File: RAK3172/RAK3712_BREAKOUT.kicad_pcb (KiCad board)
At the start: 2 copper layers, 26.9 x 52 mm, 5 parts, among them J1 Conn_01x20_Male, J2 Conn_01x20_Male, U1 RAK11300

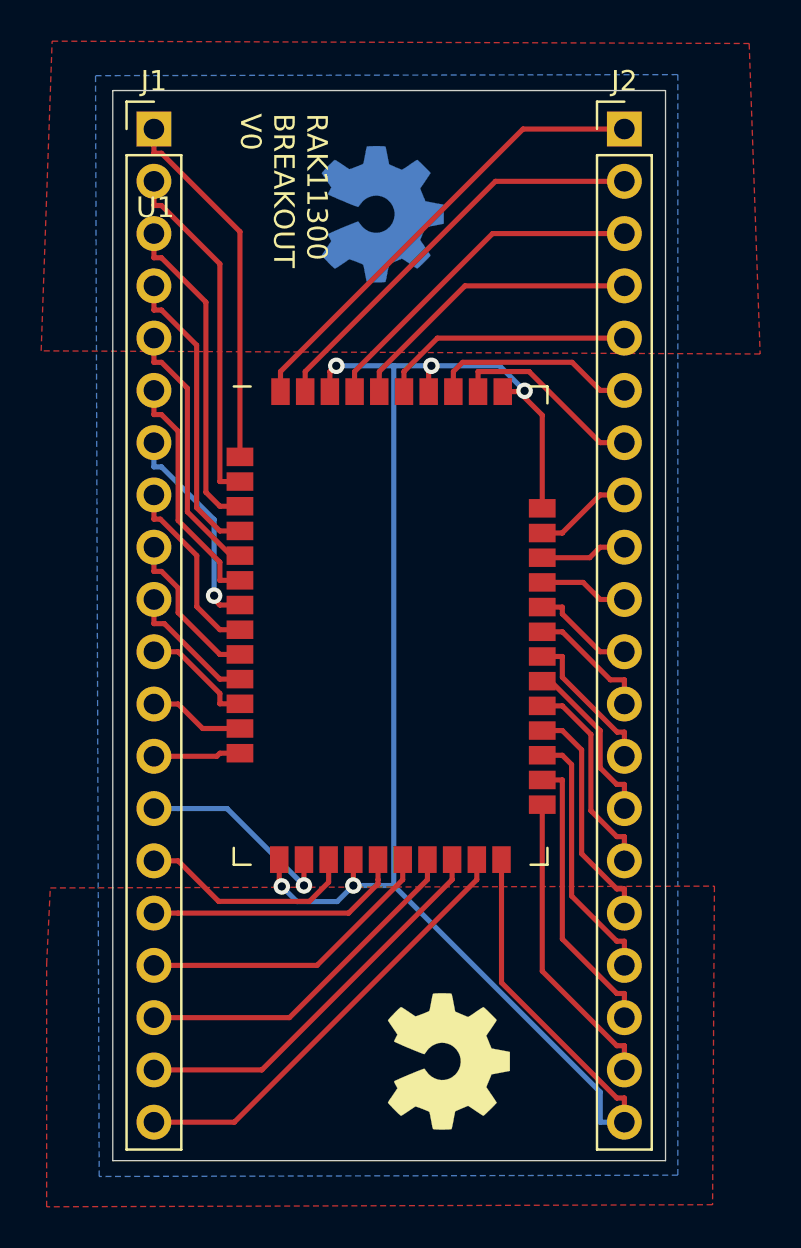
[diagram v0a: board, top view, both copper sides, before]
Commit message: foot:(DIL_BREAKOUT_PCB RAK 3712)ready for route
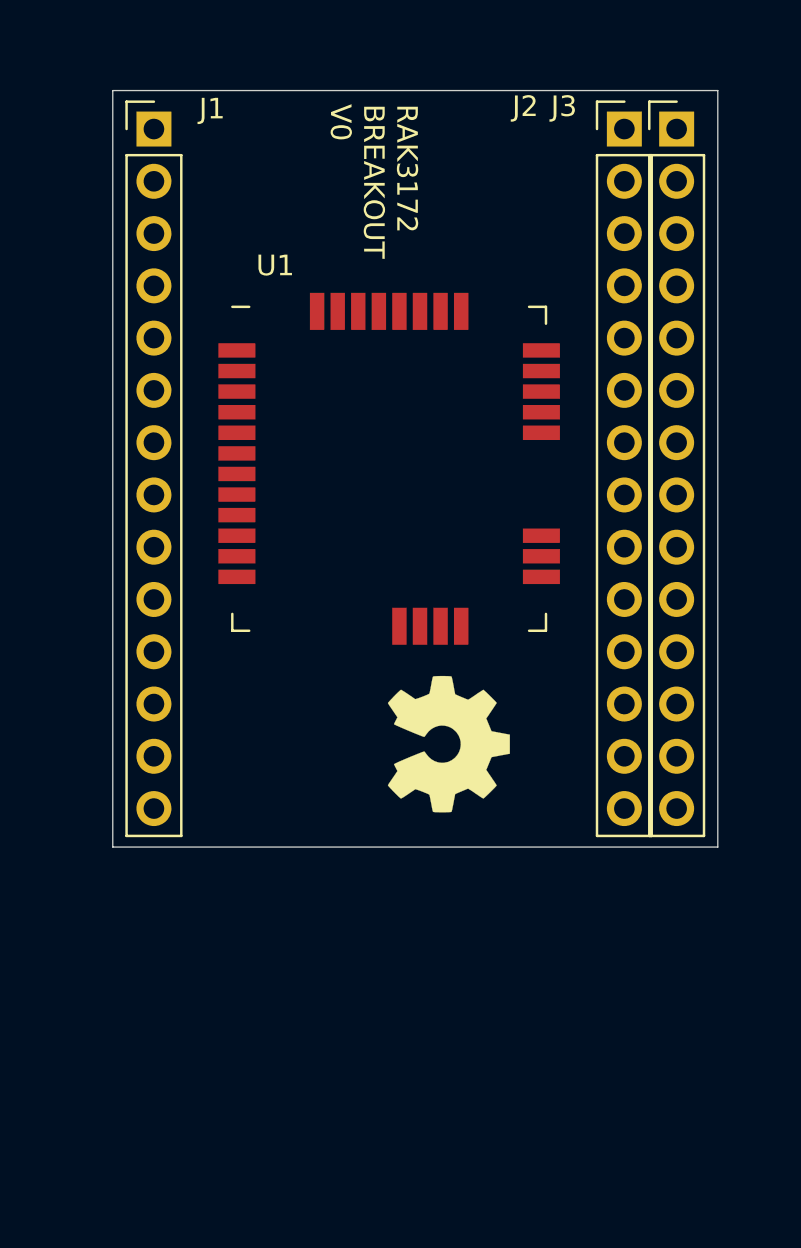
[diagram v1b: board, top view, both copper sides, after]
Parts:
- removed the REF** at (63.1, 56.0)
- added J3: Conn_01x14_Male, Connector_PinHeader_2.54mm:PinHeader_1x14_P2.54mm_Vertical, F.Cu at (77.4, 51.9)
- J1, J2: value Conn_01x20_Male -> Conn_01x14_Male; footprint Connector_PinHeader_2.54mm:PinHeader_1x20_P2.54mm_Vertical -> Connector_PinHeader_2.54mm:PinHeader_1x14_P2.54mm_Vertical
- U1: value RAK11300 -> RAK3712; footprint RAKWIRELESS:RAK11300 -> RAKWIRELESS:RAK3712
- moved REF** 15.4 mm to (66.3, 81.8)
- moved U1 7.62 mm to (63.4, 68.4)
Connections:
- J1 pad 14: /ICPIN15 -> /ICPIN14
- J2 pad 1: /ICPIN46 -> /ICPIN32
- J2 pad 10: /ICPIN33 -> /ICPIN21
- J2 pad 11: /ICPIN32 -> /ICPIN20
- J2 pad 12: /ICPIN31 -> /ICPIN19
- J2 pad 13: /ICPIN30 -> /ICPIN16
- J2 pad 14: /ICPIN29 -> /ICPIN15
- J2 pad 2: /ICPIN45 -> /ICPIN31
- J2 pad 3: /ICPIN43 -> /ICPIN30
- J2 pad 4: /ICPIN42 -> /ICPIN29
- J2 pad 5: /ICPIN41 -> /ICPIN27
- J2 pad 6: /ICPIN39 -> /ICPIN26
- J2 pad 7: /ICPIN38 -> /ICPIN25
- J2 pad 8: /ICPIN35 -> /ICPIN24
- J2 pad 9: /ICPIN34 -> /ICPIN22
- U1 pad 14: /ICPIN23 -> /ICPIN14
- U1 pad 17: /ICPIN23 -> /ICPIN11
- U1 pad 18: /ICPIN18 -> /ICPIN11
- U1 pad 23: /ICPIN23 -> /ICPIN11
- U1 pad 28: /ICPIN28 -> /ICPIN11
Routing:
- net /ICPIN23: track 85.7 -> 0.00 mm, vias 5 -> 0
- net /ICPIN46: track 22.6 -> 0.00 mm
- net /ICPIN22: track 21.5 -> 0.00 mm
- net /ICPIN45: track 20.3 -> 0.00 mm
- net /ICPIN21: track 19.3 -> 0.00 mm
- net /ICPIN01: track 17.9 -> 0.00 mm
- net /ICPIN02: track 17.1 -> 0.00 mm
- net /ICPIN20: track 17.0 -> 0.00 mm
- net /ICPIN43: track 16.9 -> 0.00 mm
- net /ICPIN03: track 15.8 -> 0.00 mm
- net /ICPIN19: track 14.8 -> 0.00 mm
- net /ICPIN24: track 14.8 -> 0.00 mm
- net /ICPIN42: track 14.6 -> 0.00 mm
- net /ICPIN04: track 14.4 -> 0.00 mm
- net /ICPIN25: track 14.0 -> 0.00 mm
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- removed copper zone on B.Cu, net /ICPIN23
- removed copper zone on F.Cu, net /ICPIN23
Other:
- board size 26.9 x 52 mm -> 29.4 x 36.8 mm
- board text added: "RAK3172 BREAKOUT V0"
- board text removed: "RAK11300 BREAKOUT V0"

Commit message: foot:(DIL_BREAKOUT_PCB RAK 3712)first route
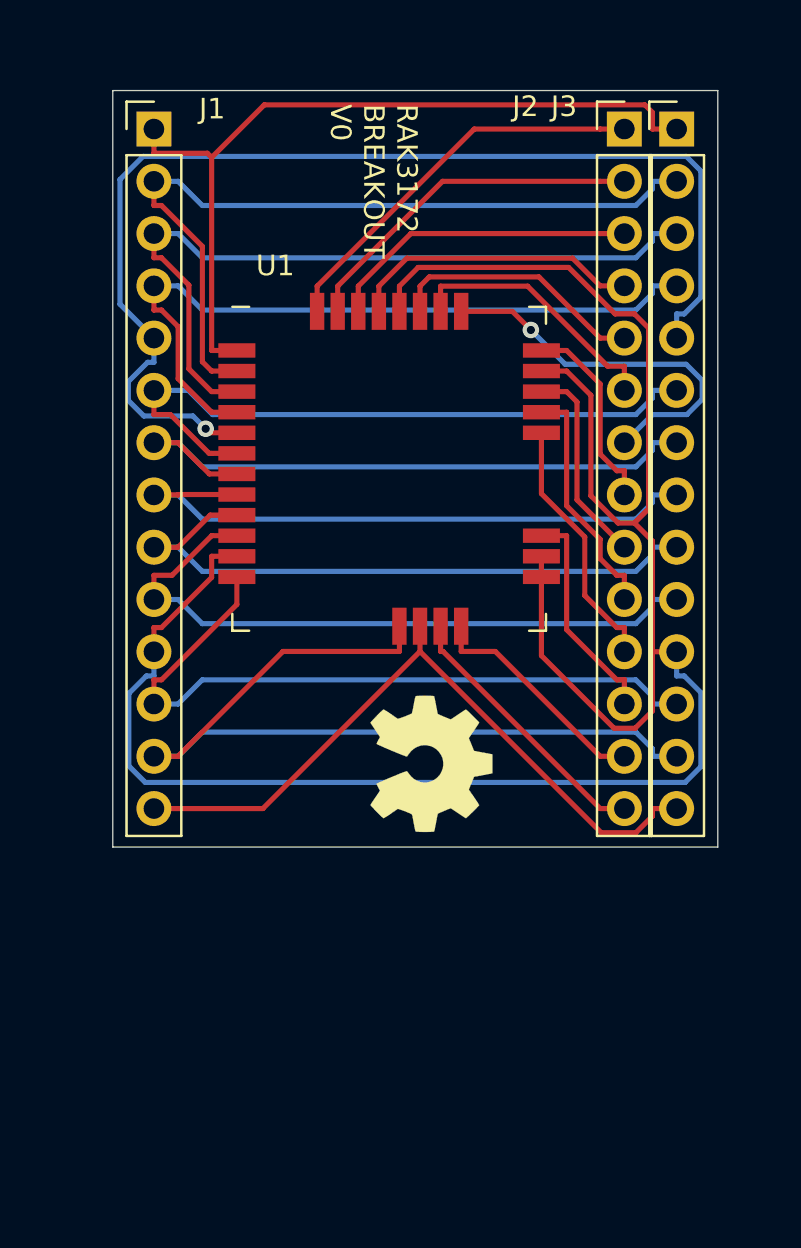
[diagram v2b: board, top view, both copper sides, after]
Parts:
- moved REF** 1.28 mm to (65.5, 82.7)
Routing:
- net /ICPIN11: track 0.00 -> 106.1 mm
- net /ICPIN05: track 0.00 -> 55.8 mm, vias 0 -> 1
- net /ICPIN13: track 0.00 -> 41.9 mm
- net /ICPIN01: track 0.00 -> 39.3 mm
- net /ICPIN02: track 0.00 -> 38.4 mm
- net /ICPIN03: track 0.00 -> 36.9 mm
- net /ICPIN04: track 0.00 -> 35.3 mm
- net /ICPIN12: track 0.00 -> 34.7 mm
- net /ICPIN14: track 0.00 -> 34.1 mm
- net /ICPIN10: track 0.00 -> 32.6 mm
- net /ICPIN06: track 0.00 -> 32.6 mm
- net /ICPIN09: track 0.00 -> 31.3 mm
- net /ICPIN07: track 0.00 -> 31.2 mm
- net /ICPIN08: track 0.00 -> 30.6 mm
- net /ICPIN32: track 0.00 -> 19.3 mm
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
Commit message: pcb:(DIL_BREAKOUT_PCB RAK 3712)routed!
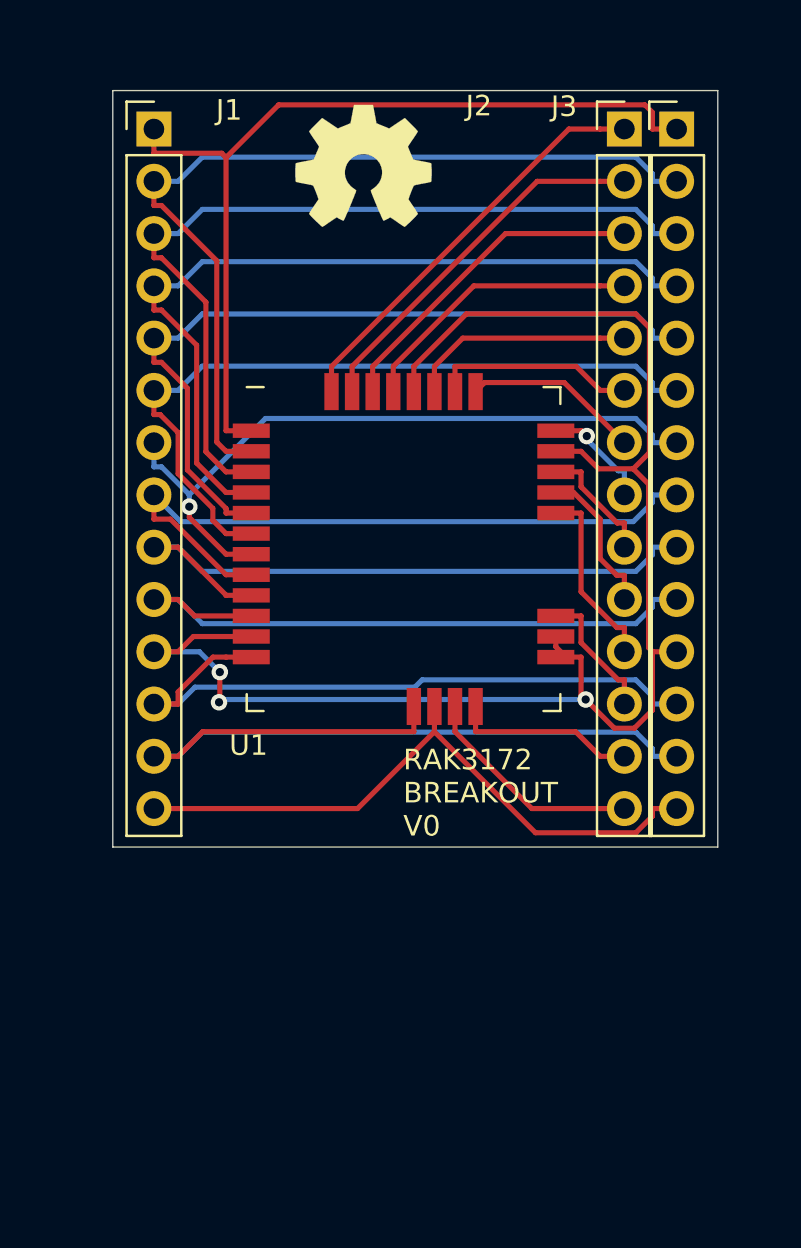
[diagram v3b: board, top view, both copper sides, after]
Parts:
- moved REF** 29.2 mm to (62.2, 53.7), turned to 0 degrees
- moved U1 3.96 mm to (64.1, 72.3)
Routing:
- net /ICPIN11: track 106.1 -> 75.4 mm, vias 0 -> 3
- net /ICPIN05: track 55.8 -> 38.0 mm, vias 1 -> 0
- net /ICPIN25: track 18.7 -> 8.62 mm, vias 1 -> 0
- net /ICPIN21: track 11.7 -> 7.30 mm
- net /ICPIN19: track 10.8 -> 6.55 mm
- net /ICPIN24: track 9.62 -> 5.40 mm, vias 0 -> 1
- net /ICPIN03: track 36.9 -> 41.1 mm
- net /ICPIN02: track 38.4 -> 42.6 mm
- net /ICPIN04: track 35.3 -> 39.5 mm
- net /ICPIN22: track 9.95 -> 5.96 mm
- net /ICPIN01: track 39.3 -> 43.2 mm
- net /ICPIN06: track 32.6 -> 36.4 mm
- net /ICPIN20: track 12.5 -> 9.05 mm
- net /ICPIN14: track 34.1 -> 30.9 mm
- net /ICPIN08: track 30.6 -> 33.7 mm
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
